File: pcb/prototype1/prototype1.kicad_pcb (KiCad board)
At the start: 2 copper layers, 96 x 96 mm, 48 parts, among them P1 USB_B, SW1 SW_PUSH, U1 STM32F410R8-LQFP64, U2 TLC5926, U3 TLC5926, U4 TLC5926

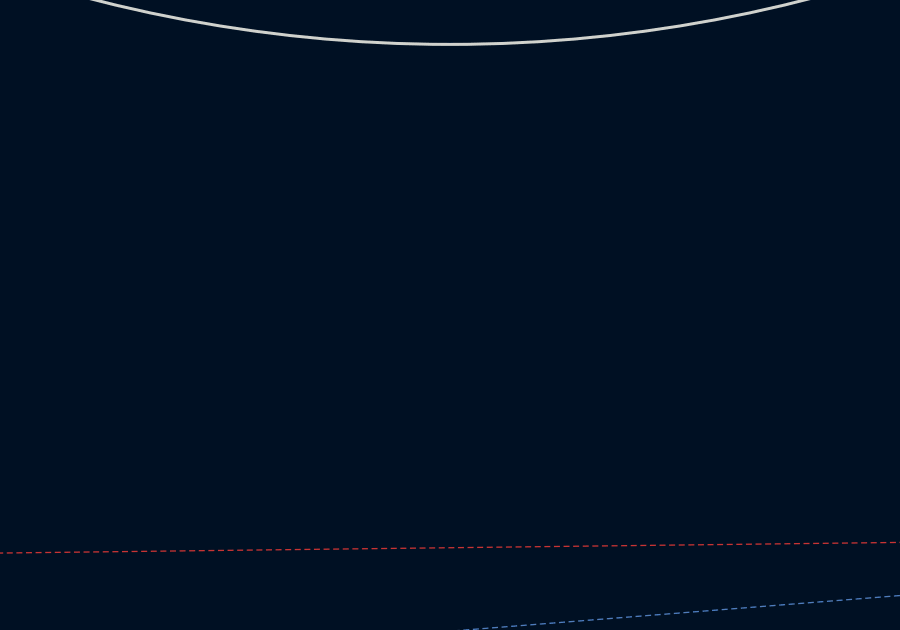
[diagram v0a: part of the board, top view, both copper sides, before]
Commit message: fix custom kicad libs
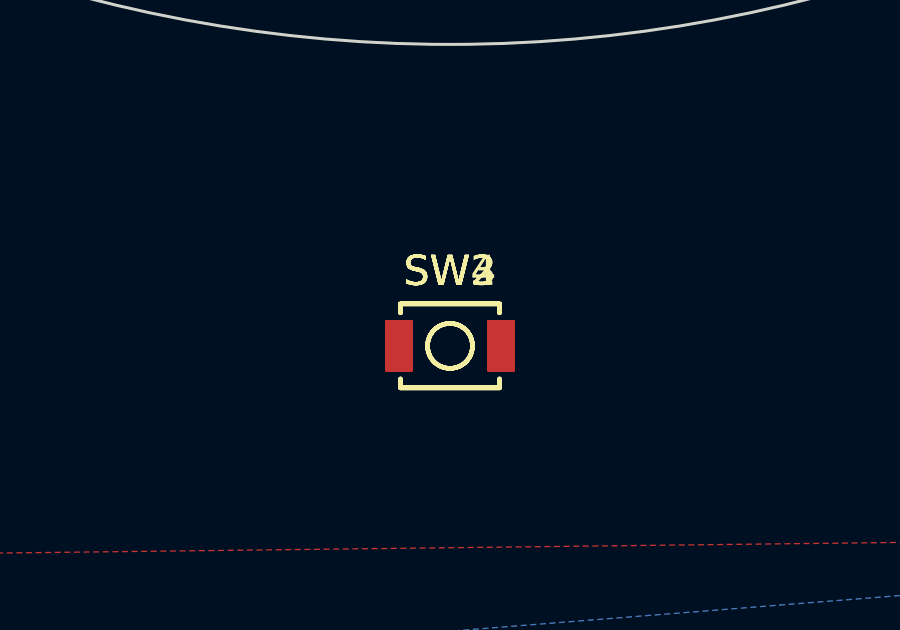
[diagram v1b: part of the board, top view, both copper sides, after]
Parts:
- added SW2: LEFT, Buttons_Switches_SMD:SW_SPST_B3U-1000P, F.Cu at (150.0, 158.1)
- added SW3: RIGHT, Buttons_Switches_SMD:SW_SPST_B3U-1000P, F.Cu at (150.0, 158.1)
- added SW4: DOWN, Buttons_Switches_SMD:SW_SPST_B3U-1000P, F.Cu at (150.0, 158.1)
- SW1: value SW_PUSH -> UP/BOOT
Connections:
- SW1 pad 1: Net-(SW1-Pad1) -> BOOT0
- U1 pad 26: Net-(U1-Pad26) -> BOOT0
- U1 pad 60: Net-(SW1-Pad1) -> BOOT0
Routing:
- net Net-(SW1-Pad1): track 4.22 -> 0.00 mm, vias 1 -> 0
- net BOOT0: track 0.00 -> 4.22 mm, vias 0 -> 1

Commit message: Working on pcb
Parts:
- added C10: 10u, Capacitors_SMD:C_0603_HandSoldering, F.Cu at (141.1, 68.9)
- added C6: 24p, Capacitors_SMD:C_0603_HandSoldering, F.Cu at (143.2, 90.0)
- added C7: 10u, Capacitors_SMD:C_0603_HandSoldering, F.Cu at (139.1, 86.4)
- added C8: 10u, Capacitors_SMD:C_0603_HandSoldering, F.Cu at (139.1, 88.2)
- added C9: 10u, Capacitors_SMD:C_0603_HandSoldering, F.Cu at (139.1, 89.9)
- added L1: 1uH 4.9mOhm, spin:SRU1028-10x10-Octogon, F.Cu at (141.1, 76.4)
- added P2: AAA1 HOT, Socket_Strips:Socket_Strip_Straight_1x01, F.Cu at (174.2, 127.2)
- added P3: AAA1 GND, Socket_Strips:Socket_Strip_Straight_1x01, F.Cu at (174.0, 73.0)
- added P4: AAA2 GND, Socket_Strips:Socket_Strip_Straight_1x01, F.Cu at (125.8, 127.2)
- added P5: AAA2 HOT, Socket_Strips:Socket_Strip_Straight_1x01, F.Cu at (126.2, 72.8)
- added R6: 316k, Resistors_SMD:R_0603_HandSoldering, F.Cu at (143.1, 88.2)
- added R7: 100k, Resistors_SMD:R_0603_HandSoldering, F.Cu at (143.1, 86.4)
- added SW5: SPST, Buttons_Switches_SMD:SW_SPST_EVQPE1, F.Cu at (142.8, 58.8)
- added U5: LM1117-3.3, TO_SOT_Packages_SMD:SOT-223, F.Cu at (150.0, 135.7)
- added U6: TPS61021, spin:WSON-8_2x2mm, F.Cu at (141.1, 84.1)
- C1, C2, C3, C4, C5, SW2, SW3, SW4: moved to B.Cu
- U1: value STM32F410R8-LQFP64 -> STM32F410R8/B; moved to B.Cu
- moved SW3 24.0 mm to (146.4, 134.3), turned to 90 degrees
- moved SW2 24.0 mm to (153.4, 134.3), turned to 90 degrees
- moved SW1 21.8 mm to (149.9, 131.8), turned to 270 degrees
- moved SW4 21.3 mm to (149.9, 136.8), turned to 90 degrees
- moved C2 14.0 mm to (160.0, 117.2), turned to 0 degrees
- moved C3 13.5 mm to (153.8, 104.0), turned to 90 degrees
- moved C5 10.9 mm to (140.5, 111.2)
- moved R2 8.95 mm to (157.5, 139.9)
- moved R1 8.34 mm to (142.8, 139.5)
- moved C4 6.58 mm to (147.2, 104.0)
- moved U1 6.42 mm to (150.0, 113.5)
- moved C1 5.84 mm to (146.2, 124.0)
- moved P1 0.27 mm to (150.0, 143.6)
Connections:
- net ADC1 renamed Net-(U1-Pad15)
- net ADC2 renamed Net-(U1-Pad16)
- net ADC3 renamed Net-(U1-Pad17)
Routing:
- net Net-(P2-Pad1): track 0.00 -> 48.5 mm
- net Net-(C10-Pad2): track 0.00 -> 31.1 mm
- net Net-(R2-Pad2): track 27.7 -> 0.00 mm, vias 2 -> 0
- net Net-(P5-Pad1): track 0.00 -> 25.7 mm
- net Net-(R1-Pad2): track 24.6 -> 0.00 mm
- net GND: track 6.99 -> 29.7 mm, vias 10 -> 6
- net VCC: track 40.2 -> 49.4 mm, vias 17 -> 24
- net Net-(C6-Pad1): track 0.00 -> 6.72 mm
- net BOOT0: track 4.22 -> 0.00 mm, vias 1 -> 0
- net Net-(P1-Pad3): track 3.00 -> 0.00 mm, vias 1 -> 0
- net Net-(P1-Pad2): track 2.84 -> 0.00 mm, vias 1 -> 0
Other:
- net class Wide added: clearance 0.4, trace_width 0.75, via_dia 0.8, via_drill 0.6

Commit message: More pcb changes
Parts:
- P2, P3, P4, P5: moved to B.Cu
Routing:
- net GND: track 29.7 -> 33.1 mm

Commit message: More pcb stuff
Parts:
- added REF**: 1pin, Connect:1pin, F.Cu at (183.5, 100.0)
- added REF**: 1pin, Connect:1pin, F.Cu at (163.8, 100.0)
- added REF**: 1pin, Connect:1pin, F.Cu at (116.2, 100.0)
- added REF**: 1pin, Connect:1pin, F.Cu at (136.2, 100.0)
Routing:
- net VCC: track 49.4 -> 88.0 mm, vias 24 -> 23
- net GND: vias 6 -> 5
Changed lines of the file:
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@@
 (kicad_pcb (version 4) (host pcbnew 4.0.2-stable)
   (general
-    (links 218)
+    (links 0)
     (no_connects 39)
     (area 101.949999 51.949999 198.050001 148.050001)
     (thickness 1.6)
     (drawings 19)
-    (tracks 548)
+    (tracks 574)
     (zones 0)
-    (modules 66)
+    (modules 70)
     (nets 115)
   )
@@
     (pad_drill 0.6)
     (pad_to_mask_clearance 0)
-    (aux_axis_origin 0 0)
+    (aux_axis_origin 979.25 -51.2)
     (visible_elements FFFEFF7F)
     (pcbplotparams
@@
     (uvia_drill 0.2)
   )
+  (module Connect:1pin (layer F.Cu)
+    (at 183.5 100)
+    (descr "module 1 pin (ou trou mecanique de percage)")
+    (tags DEV)
+    (fp_text reference REF** (at 0 -3.048) (layer F.SilkS) hide
+      (effects (font (size 1 1) (thickness 0.15)))
+    )
+    (fp_text value 1pin (at 0 2.794) (layer F.Fab)
+      (effects (font (size 1 1) (thickness 0.15)))
+    )
+    (fp_circle (center 0 0) (end 0 -2.286) (layer F.SilkS) (width 0.15))
+    (pad 1 thru_hole circle (at 0 0) (size 4.064 4.064) (drill 3.048) (layers *.Cu *.Mask F.SilkS))
+  )
+  (module Connect:1pin (layer F.Cu)
+    (at 163.75 100)
+    (descr "module 1 pin (ou trou mecanique de percage)")
+    (tags DEV)
+    (fp_text reference REF** (at 0 -3.048) (layer F.SilkS) hide
+      (effects (font (size 1 1) (thickness 0.15)))
+    )
+    (fp_text value 1pin (at 0 2.794) (layer F.Fab)
+      (effects (font (size 1 1) (thickness 0.15)))
+    )
+    (fp_circle (center 0 0) (end 0 -2.286) (layer F.SilkS) (width 0.15))
+    (pad 1 thru_hole circle (at 0 0) (size 4.064 4.064) (drill 3.048) (layers *.Cu *.Mask F.SilkS))
+  )
+  (module Connect:1pin (layer F.Cu)
+    (at 116.25 100)
+    (descr "module 1 pin (ou trou mecanique de percage)")
+    (tags DEV)
+    (fp_text reference REF** (at 0 -3.048) (layer F.SilkS) hide
+      (effects (font (size 1 1) (thickness 0.15)))
+    )
+    (fp_text value 1pin (at 0 2.794) (layer F.Fab)
+      (effects (font (size 1 1) (thickness 0.15)))
+    )
+    (fp_circle (center 0 0) (end 0 -2.286) (layer F.SilkS) (width 0.15))
+    (pad 1 thru_hole circle (at 0 0) (size 4.064 4.064) (drill 3.048) (layers *.Cu *.Mask F.SilkS))
+  )
   (module Housings_QFP:TQFP-64_10x10mm_Pitch0.5mm (layer B.Cu)
     (at 150 113.5)
@@
     )
   )
+  (module Connect:1pin (layer F.Cu)
+    (at 136.25 100)
+    (descr "module 1 pin (ou trou mecanique de percage)")
+    (tags DEV)
+    (fp_text reference REF** (at 0 -3.048) (layer F.SilkS) hide
+      (effects (font (size 1 1) (thickness 0.15)))
+    )
+    (fp_text value 1pin (at 0 2.794) (layer F.Fab)
+      (effects (font (size 1 1) (thickness 0.15)))
+    )
+    (fp_circle (center 0 0) (end 0 -2.286) (layer F.SilkS) (width 0.15))
+    (pad 1 thru_hole circle (at 0 0) (size 4.064 4.064) (drill 3.048) (layers *.Cu *.Mask F.SilkS))
+  )
   (gr_arc (start 123 77.5) (end 120 77.5) (angle 90) (layer Edge.Cuts) (width 0.1))
   (gr_line (start 120 122.5) (end 120 77.5) (layer Edge.Cuts) (width 0.1))
@@
   (gr_line (start 150 102.75) (end 150 98.25) (layer Eco1.User) (width 0.2))
   (segment (start 149.299348 136.618206) (end 149.249346 136.618206) (width 0.25) (layer B.Cu) (net 0) (status 30))
+  (segment (start 149.125736 55.5) (end 147.5 55.5) (width 0.25) (layer F.Cu) (net 1))
+  (segment (start 149.95 55.1) (end 149.525736 55.1) (width 0.25) (layer F.Cu) (net 1))
+  (segment (start 149.525736 55.1) (end 149.125736 55.5) (width 0.25) (layer F.Cu) (net 1))
+  (segment (start 149.475736 58.5) (end 147.5 58.5) (width 0.25) (layer F.Cu) (net 1))
+  (segment (start 150 58.4) (end 149.575736 58.4) (width 0.25) (layer F.Cu) (net 1))
+  (segment (start 149.575736 58.4) (end 149.475736 58.5) (width 0.25) (layer F.Cu) (net 1))
+  (segment (start 149.95 61.5) (end 147.5 61.5) (width 0.25) (layer F.Cu) (net 1))
+  (segment (start 150 64.45) (end 147.55 64.45) (width 0.25) (layer F.Cu) (net 1))
+  (segment (start 149.475736 67.5) (end 147.5 67.5) (width 0.25) (layer F.Cu) (net 1))
+  (segment (start 149.95 67.45) (end 149.525736 67.45) (width 0.25) (layer F.Cu) (net 1))
+  (segment (start 149.525736 67.45) (end 149.475736 67.5) (width 0.25) (layer F.Cu) (net 1))
+  (segment (start 149.475736 70.5) (end 147.75 70.5) (width 0.25) (layer F.Cu) (net 1))
+  (segment (start 150 70.4) (end 149.575736 70.4) (width 0.25) (layer F.Cu) (net 1))
+  (segment (start 149.575736 70.4) (end 149.475736 70.5) (width 0.25) (layer F.Cu) (net 1))
+  (segment (start 150 73.45) (end 147.55 73.45) (width 0.25) (layer F.Cu) (net 1))
+  (segment (start 150 76.45) (end 147.8 76.45) (width 0.25) (layer F.Cu) (net 1))
+  (segment (start 150 79.5) (end 147.5 79.5) (width 0.25) (layer F.Cu) (net 1))
+  (segment (start 150 82.5) (end 147.5 82.5) (width 0.25) (layer F.Cu) (net 1))
+  (segment (start 150 85.45) (end 147.55 85.45) (width 0.25) (layer F.Cu) (net 1))
+  (segment (start 150 88.5) (end 147.5 88.5) (width 0.25) (layer F.Cu) (net 1))
+  (segment (start 149.575736 91.5) (end 147.5 91.5) (width 0.25) (layer F.Cu) (net 1))
+  (segment (start 150 91.5) (end 149.575736 91.5) (width 0.25) (layer F.Cu) (net 1))
+  (segment (start 150 97.5) (end 147.5 97.5) (width 0.25) (layer F.Cu) (net 1))
+  (segment (start 149.575736 94.5) (end 147.5 94.5) (width 0.25) (layer F.Cu) (net 1))
+  (segment (start 150 94.5) (end 149.575736 94.5) (width 0.25) (layer F.Cu) (net 1))
+  (segment (start 148.6 99.7) (end 149.2 99.7) (width 0.25) (layer B.Cu) (net 1))
+  (segment (start 149.2 99.7) (end 150 98.9) (width 0.25) (layer B.Cu) (net 1))
+  (segment (start 150 97.924264) (end 150 97.5) (width 0.25) (layer B.Cu) (net 1))
+  (segment (start 150 98.9) (end 150 97.924264) (width 0.25) (layer B.Cu) (net 1))
   (via (at 153.448448 132.580746) (size 0.6) (drill 0.4) (layers F.Cu B.Cu) (net 1))
   (via (at 146.4 132.580746) (size 0.6) (drill 0.4) (layers F.Cu B.Cu) (net 1))
@@
   (segment (start 141.981449 88.179035) (end 140.581449 88.179035) (width 0.75) (layer F.Cu) (net 1) (status 30))
   (segment (start 148.6 99.7) (end 148.8 99.7) (width 0.25) (layer B.Cu) (net 1) (status 30))
-  (segment (start 148.8 99.7) (end 149.8 100.7) (width 0.25) (layer B.Cu) (net 1) (status 10))
-  (via (at 149.8 100.7) (size 0.6) (drill 0.4) (layers F.Cu B.Cu) (net 1))
   (segment (start 148.6 96.7) (end 149.2 96.7) (width 0.25) (layer B.Cu) (net 1) (status 10))
   (segment (start 149.2 96.7) (end 150 97.5) (width 0.25) (layer B.Cu) (net 1))
@@
   (via (at 138.131449 88.179035) (size 0.6) (drill 0.4) (layers F.Cu B.Cu) (net 2) (status 30))
   (via (at 138.131449 86.429035) (size 0.6) (drill 0.4) (layers F.Cu B.Cu) (net 2) (status 30))
-  (via (at 141.081449 84.129035) (size 0.6) (drill 0.4) (layers F.Cu B.Cu) (net 2) (status 30))
   (via (at 141.081449 67.979035) (size 0.6) (drill 0.4) (layers F.Cu B.Cu) (net 2) (status 30))
   (segment (start 141.97 85.079035) (end 143.531449 85.079035) (width 0.75) (layer F.Cu) (net 2) (status 10))

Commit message: More pcb changes
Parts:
- added C11: 100n, Capacitors_SMD:C_0603_HandSoldering, F.Cu at (152.2, 133.8)
- added C12: 10u, Capacitors_SMD:C_0603_HandSoldering, F.Cu at (150.0, 133.8)
- added REF**: 1pin, Connect:1pin, F.Cu at (155.0, 100.0)
- added REF**: 1pin, Connect:1pin, F.Cu at (145.0, 100.0)
- added U7: L3GD20HTR, spin:L3GD20H, F.Cu at (150.0, 118.0)
- added U8: LIS331HH, spin:LGA16, F.Cu at (140.5, 100.0)
- added U9: LIS331HH, spin:LGA16, F.Cu at (159.5, 100.0)
- C1, C2, C3, C4: footprint Capacitors_SMD:C_0805_HandSoldering -> Capacitors_SMD:C_0603_HandSoldering
- LED1, LED10, LED11, LED12, LED13, LED14, LED15, LED16, LED17, LED18, LED19, LED2, LED20, LED21, LED22, LED23, LED24, LED25, LED26, LED27, LED28, LED29, LED3, LED30, LED31, LED32, LED4, LED5, LED6, LED7, LED8, LED9: footprint spinny:LED_CLV1L-PLCC4 -> spin:LED_CLV1L-PLCC4
- P1: footprint Connect:USB_Micro-B -> spin:ZX62M-B-5P; moved to F.Cu
- R1, R2: footprint Resistors_SMD:R_0805_HandSoldering -> Resistors_SMD:R_0603_HandSoldering
- R3, R4, R5: footprint Resistors_SMD:R_0805_HandSoldering -> Resistors_ThroughHole:Resistor_Vertical_RM5mm
- SW1: value UP/BOOT -> Boot Button; footprint Buttons_Switches_SMD:SW_SPST_B3U-1000P -> spin:Button
- SW2: value LEFT -> Button; footprint Buttons_Switches_SMD:SW_SPST_B3U-1000P -> spin:Button
- SW3: value RIGHT -> Button; footprint Buttons_Switches_SMD:SW_SPST_B3U-1000P -> spin:Button
- SW4: value DOWN -> Button; footprint Buttons_Switches_SMD:SW_SPST_B3U-1000P -> spin:Button
- U5: value LM1117-3.3 -> LD1117S33CTR
- moved SW4 10.6 mm to (159.0, 131.2), turned to 0 degrees
- moved U5 8.45 mm to (150.0, 127.2)
- moved C1 6.45 mm to (141.0, 120.2)
- moved SW3 6.19 mm to (141.0, 131.2), turned to 180 degrees
- moved SW1 5.05 mm to (150.0, 126.8), turned to 90 degrees
- moved R3 4.98 mm to (135.8, 81.8)
- moved SW2 3.75 mm to (150.0, 135.8), turned to 270 degrees
- moved P1 2.40 mm to (150.0, 146.0), turned to 0 degrees
- moved REF** 1.25 mm to (165.0, 100.0)
- moved REF** 1.25 mm to (135.0, 100.0)
- moved R4 1.13 mm to (161.0, 84.0)
- moved R5 0.96 mm to (160.8, 68.8)
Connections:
- U1 pad 24: Net-(U1-Pad24) -> SS_GYRO
- U1 pad 25: Net-(U1-Pad25) -> SS_ACC1
- U1 pad 30: Net-(U1-Pad30) -> VCC
- U1 pad 37: Net-(U1-Pad37) -> SS_ACC2
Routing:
- net Net-(R4-Pad2): track 4.46 -> 0.00 mm
- net Net-(R5-Pad2): track 4.44 -> 0.00 mm
- net Net-(R3-Pad2): track 3.94 -> 0.00 mm
- net VCC: track 88.0 -> 85.7 mm, vias 23 -> 19
- net B16: track 26.3 -> 24.2 mm, vias 1 -> 2
